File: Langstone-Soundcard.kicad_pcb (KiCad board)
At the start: 2 copper layers, 66.7 x 66.7 mm, 27 parts, among them J1 NF_IN, J2 USB, J3 NF_OUT, SW1 HID, U1 PCM2902, Y1 12MHz

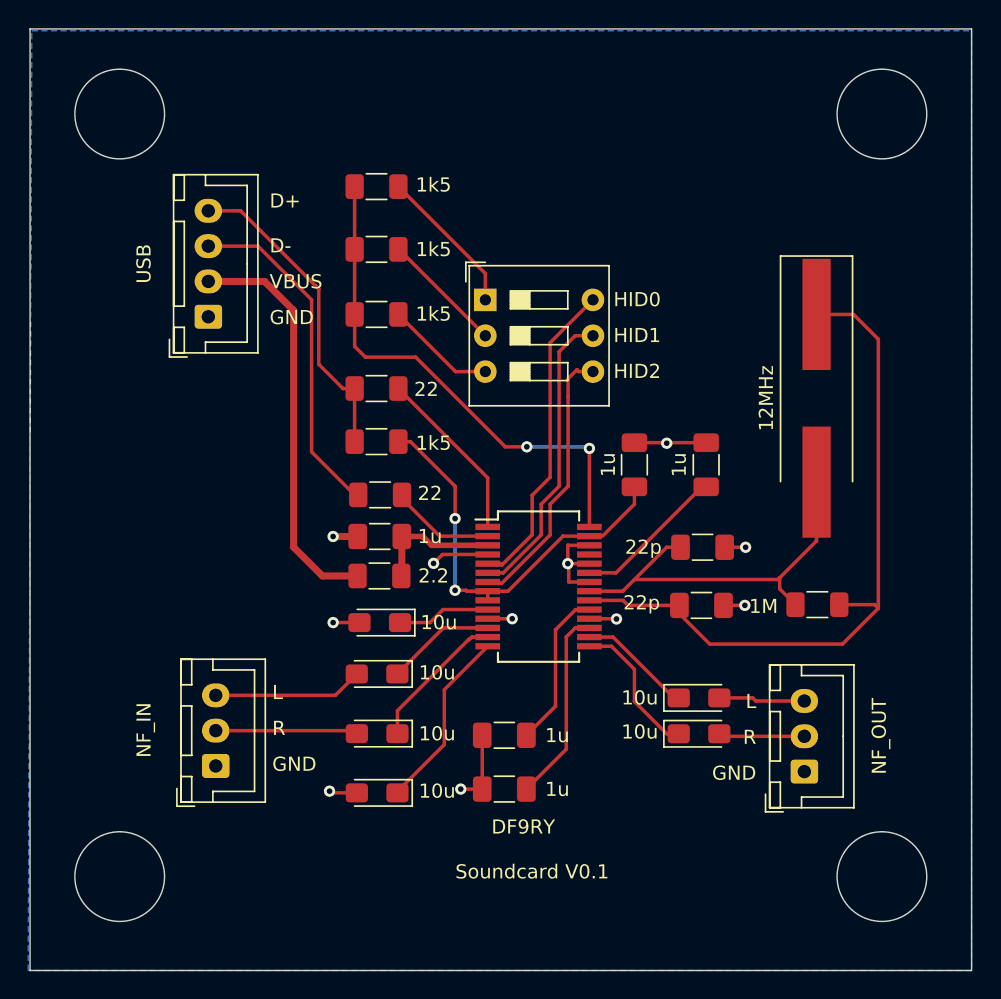
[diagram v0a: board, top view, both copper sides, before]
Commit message: 22pF auf 10pF geändert, Footprints auf SMD0805 geändert, SMD Quartz, SMD-Pin Regler auf SMD geändert. Stecker auf PH2.0 geändert.
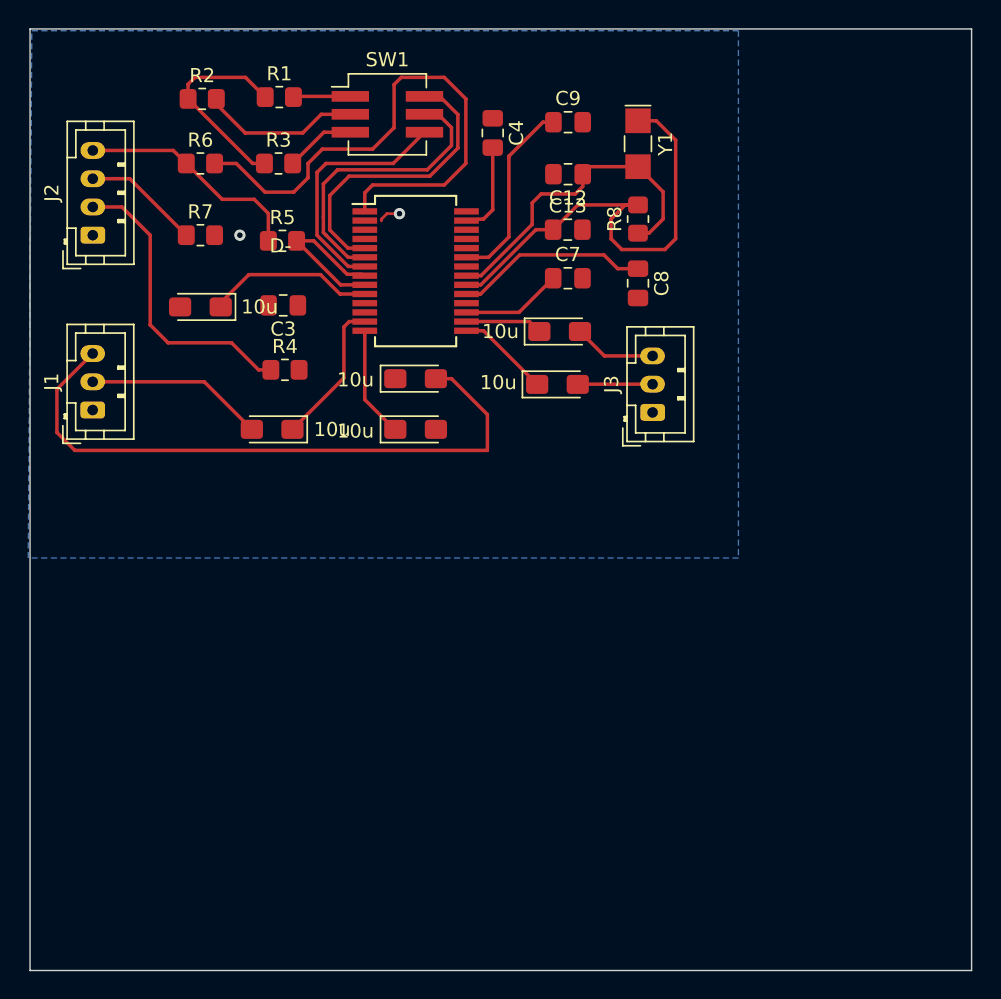
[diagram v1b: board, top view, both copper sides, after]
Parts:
- C12, C13: value 22p -> 10p; footprint Capacitor_SMD:C_1206_3216Metric_Pad1.33x1.80mm_HandSolder -> Capacitor_SMD:C_0805_2012Metric_Pad1.18x1.45mm_HandSolder
- C3, C4, C7, C8, C9: footprint Capacitor_SMD:C_1206_3216Metric_Pad1.33x1.80mm_HandSolder -> Capacitor_SMD:C_0805_2012Metric_Pad1.18x1.45mm_HandSolder
- J1, J3: footprint Connector_JST:JST_XH_B3B-XH-A_1x03_P2.50mm_Vertical -> Connector_JST:JST_PH_B3B-PH-K_1x03_P2.00mm_Vertical
- J2: footprint Connector_JST:JST_XH_B4B-XH-A_1x04_P2.50mm_Vertical -> Connector_JST:JST_PH_B4B-PH-K_1x04_P2.00mm_Vertical
- R1, R2, R3, R4, R5, R6, R7, R8: footprint Resistor_SMD:R_1206_3216Metric_Pad1.30x1.75mm_HandSolder -> Resistor_SMD:R_0805_2012Metric_Pad1.20x1.40mm_HandSolder
- SW1: footprint Button_Switch_THT:SW_DIP_SPSTx03_Slide_9.78x9.8mm_W7.62mm_P2.54mm -> Button_Switch_SMD:SW_DIP_SPSTx03_Slide_KingTek_DSHP03TJ_W5.25mm_P1.27mm_JPin
- Y1: footprint Crystal:Crystal_SMD_HC49-SD_HandSoldering -> Crystal:Crystal_SMD_G8-2Pin_3.2x1.5mm_HandSoldering
- moved C7 36.5 mm to (130.2, 71.6), turned to 0 degrees
- moved C8 33.4 mm to (135.1, 72.0), turned to -90 degrees
- moved R8 30.1 mm to (135.1, 67.4), turned to 90 degrees
- moved C13 28.2 mm to (130.2, 68.2)
- moved C12 28.1 mm to (130.2, 64.3), turned to 180 degrees
- moved C10 27.8 mm to (129.6, 75.4)
- moved J3 27.6 mm to (136.2, 81.1)
- moved C11 26.7 mm to (129.4, 79.1)
- moved J1 26.7 mm to (96.5, 81.0)
- moved C9 26.2 mm to (130.2, 60.6), turned to 0 degrees
- moved C6 25.9 mm to (119.4, 82.3), turned to 0 degrees
- moved C5 25.7 mm to (104.1, 73.7)
- moved C4 25.5 mm to (124.8, 61.3)
- moved U1 24.0 mm to (119.4, 71.1)
- moved C2 22.8 mm to (109.2, 82.3)
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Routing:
- net Net-(C1-Pad2): track 10.6 -> 44.9 mm
- net GND: track 33.9 -> 0.00 mm, vias 11 -> 0
- net Net-(R6-Pad2): track 12.4 -> 38.9 mm
- net Net-(R1-Pad1): track 36.5 -> 14.6 mm, vias 2 -> 0
- net Net-(C13-Pad1): track 50.2 -> 33.6 mm
- net Net-(J2-Pad3): track 24.0 -> 8.28 mm
- net Net-(C4-Pad2): track 28.9 -> 17.4 mm, vias 2 -> 0
- net VCC: track 9.15 -> 0.00 mm
- net Net-(J2-Pad2): track 29.0 -> 21.1 mm
- net Net-(C1-Pad1): track 7.75 -> 0.00 mm
- net Net-(R7-Pad2): track 7.53 -> 0.00 mm
- net Net-(C7-Pad1): track 13.8 -> 7.14 mm
- net Net-(J2-Pad4): track 22.5 -> 16.2 mm
- net Net-(R1-Pad2): track 10.6 -> 4.51 mm
- net Net-(C5-Pad1): track 6.59 -> 11.9 mm
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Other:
- outline, holes or cut-outs redrawn
- board text removed: "D+"
- board text removed: "DF9RY"
- board text removed: "GND"
- board text removed: "HID0"
- board text removed: "HID1"
- board text removed: "HID2"
- board text removed: "L"
- board text removed: "R"
- board text removed: "Soundcard V0.1"
- board text removed: "VBUS"

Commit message: Jemi's Verkleinerung fertig
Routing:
- net GND: track 0.00 -> 42.1 mm, vias 0 -> 10
- net Net-(R1-Pad1): track 14.6 -> 39.2 mm
- net Net-(R7-Pad2): track 0.00 -> 19.4 mm, vias 0 -> 2
- net Net-(C1-Pad2): track 44.9 -> 26.3 mm, vias 0 -> 2
- net VCC: track 0.00 -> 17.9 mm, vias 0 -> 2
- net Net-(C1-Pad1): track 0.00 -> 6.24 mm
- net Net-(C4-Pad2): track 17.4 -> 21.8 mm, vias 0 -> 2
- net (no net): track 1.56 -> 0.00 mm, vias 2 -> 0
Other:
- board size 66.7 x 66.7 mm -> 50.4 x 37.7 mm
- board text added: "D+"
- board text added: "GND"
- board text added: "L"
- board text added: "R"
- board text added: "VBUS"
